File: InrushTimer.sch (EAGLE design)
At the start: 71 parts, among them IC2 TLC272D, IC3 4076N, IC6 555, Q2 TIP41C

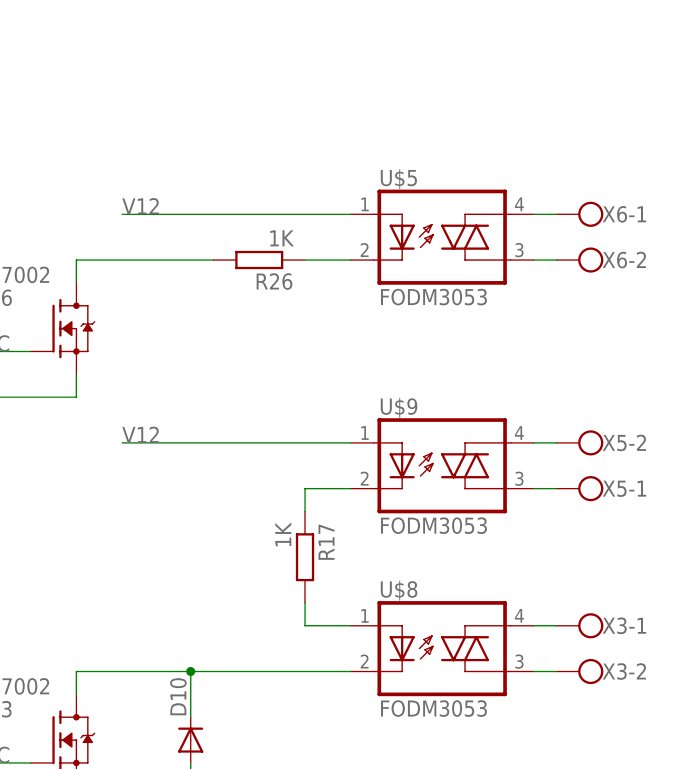
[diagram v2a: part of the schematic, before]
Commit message: Updated optotriac symbol
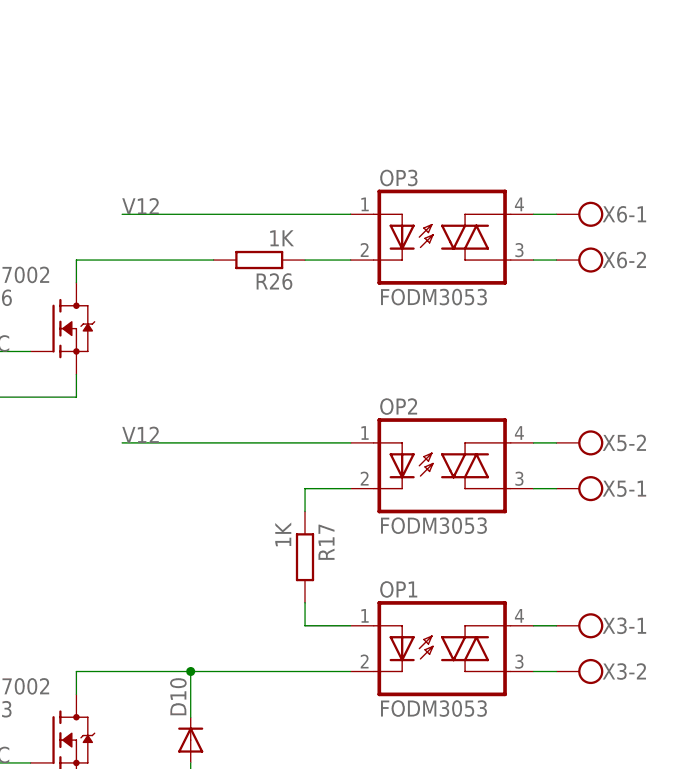
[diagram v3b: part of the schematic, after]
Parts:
- renumbered U$5 to OP3, U$8 to OP1, U$9 to OP2
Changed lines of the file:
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@@
 <part name="C4" library="rcl" deviceset="C-EU" device="050-024X044" value="100nF"/>
 <part name="C13" library="rcl" deviceset="C-EU" device="C1206K" value="100nF"/>
-<part name="U$5" library="SHoleLib" deviceset="FODM3053" device=""/>
 <part name="Q2" library="transistor-power" deviceset="TIP41C" device=""/>
 <part name="R17" library="rcl" deviceset="R-EU_" device="R0805" value="1K"/>
@@
 <part name="R24" library="rcl" deviceset="R-EU_" device="0207/7" value="51K"/>
 <part name="C11" library="rcl" deviceset="C-EU" device="050-024X044" value="100nF"/>
-<part name="U$8" library="SHoleLib" deviceset="FODM3053" device=""/>
 <part name="R25" library="pot" deviceset="TRIM_EU-" device="CA6H_MOD" value="220K"/>
 <part name="X3" library="con-wago-500" deviceset="W237-102" device=""/>
@@
 <part name="C3" library="rcl" deviceset="C-EU" device="050-024X044" value="100nF"/>
 <part name="IC6" library="linear" deviceset="*555" device=""/>
-<part name="U$9" library="SHoleLib" deviceset="FODM3053" device=""/>
 <part name="C7" library="rcl" deviceset="C-EU" device="C0805K" value="1nF"/>
 <part name="T2" library="transistor" deviceset="*-NPN-" device="SOT23-BEC" technology="MMBTA42LT1"/>
@@
 <part name="R18" library="rcl" deviceset="R-EU_" device="0207/2V" value="100R"/>
 <part name="R20" library="rcl" deviceset="R-EU_" device="0207/2V" value="10K"/>
+<part name="OP1" library="SHoleLib" deviceset="FODM3053" device=""/>
+<part name="OP2" library="SHoleLib" deviceset="FODM3053" device=""/>
+<part name="OP3" library="SHoleLib" deviceset="FODM3053" device=""/>
 </parts>
 <sheets>
@@
 <instance part="C4" gate="G$1" x="78.74" y="40.64"/>
 <instance part="C13" gate="G$1" x="132.08" y="106.68"/>
-<instance part="U$5" gate="G$1" x="518.16" y="27.94"/>
 <instance part="Q2" gate="1" x="83.82" y="50.8"/>
 <instance part="R17" gate="G$1" x="502.92" y="-7.62" rot="R270"/>
@@
 <instance part="R24" gate="G$1" x="292.1" y="-15.24" rot="R270"/>
 <instance part="C11" gate="G$1" x="226.06" y="-50.8"/>
-<instance part="U$8" gate="G$1" x="518.16" y="-17.78"/>
 <instance part="R25" gate="1" x="248.92" y="-35.56" rot="R90"/>
 <instance part="X3" gate="-1" x="535.94" y="-15.24" rot="R180"/>
@@
 <instance part="C3" gate="G$1" x="327.66" y="-10.16"/>
 <instance part="IC6" gate="A" x="210.82" y="-22.86"/>
-<instance part="U$9" gate="G$1" x="518.16" y="2.54"/>
 <instance part="C7" gate="G$1" x="119.38" y="124.46" rot="R90"/>
 <instance part="T2" gate="G$1" x="15.24" y="-5.08" smashed="yes">
@@
 <instance part="R18" gate="G$1" x="71.12" y="-20.32" rot="R180"/>
 <instance part="R20" gate="G$1" x="154.94" y="139.7"/>
+<instance part="OP1" gate="G$1" x="518.16" y="-17.78"/>
+<instance part="OP2" gate="G$1" x="518.16" y="2.54"/>
+<instance part="OP3" gate="G$1" x="518.16" y="27.94"/>
 </instances>
 <busses>
@@
 </segment>
 <segment>
-<pinref part="U$5" gate="G$1" pin="A"/>
 <wire x1="508" y1="30.48" x2="482.6" y2="30.48" width="0.1524" layer="91"/>
 <label x="482.6" y="30.48" size="1.778" layer="95"/>
+<pinref part="OP3" gate="G$1" pin="A"/>
 </segment>
 <segment>
@@
 </segment>
 <segment>
-<pinref part="U$9" gate="G$1" pin="A"/>
 <wire x1="508" y1="5.08" x2="482.6" y2="5.08" width="0.1524" layer="91"/>
 <label x="482.6" y="5.08" size="1.778" layer="95"/>
+<pinref part="OP2" gate="G$1" pin="A"/>
 </segment>
 </net>
@@
 <wire x1="490.22" y1="-20.32" x2="477.52" y2="-20.32" width="0.1524" layer="91"/>
 <wire x1="490.22" y1="-25.4" x2="490.22" y2="-20.32" width="0.1524" layer="91"/>
-<pinref part="U$8" gate="G$1" pin="C"/>
 <wire x1="490.22" y1="-20.32" x2="508" y2="-20.32" width="0.1524" layer="91"/>
 <junction x="490.22" y="-20.32"/>
+<pinref part="OP1" gate="G$1" pin="C"/>
 </segment>
 </net>
@@
 <segment>
 <pinref part="X6" gate="-2" pin="KL"/>
-<pinref part="U$5" gate="G$1" pin="A1"/>
 <wire x1="530.86" y1="25.4" x2="528.32" y2="25.4" width="0.1524" layer="91"/>
+<pinref part="OP3" gate="G$1" pin="A1"/>
 </segment>
 </net>
@@
 <segment>
 <pinref part="X6" gate="-1" pin="KL"/>
-<pinref part="U$5" gate="G$1" pin="A2"/>
 <wire x1="530.86" y1="30.48" x2="528.32" y2="30.48" width="0.1524" layer="91"/>
+<pinref part="OP3" gate="G$1" pin="A2"/>
 </segment>
 </net>
 <net name="N$18" class="0">
 <segment>
-<pinref part="U$5" gate="G$1" pin="C"/>
 <pinref part="R26" gate="G$1" pin="1"/>
 <wire x1="508" y1="25.4" x2="502.92" y2="25.4" width="0.1524" layer="91"/>
+<pinref part="OP3" gate="G$1" pin="C"/>
 </segment>
 </net>
@@
 <segment>
 <pinref part="X3" gate="-1" pin="KL"/>
-<pinref part="U$8" gate="G$1" pin="A2"/>
 <wire x1="528.32" y1="-15.24" x2="530.86" y2="-15.24" width="0.1524" layer="91"/>
+<pinref part="OP1" gate="G$1" pin="A2"/>
 </segment>
 </net>
@@
 <segment>
 <pinref part="X3" gate="-2" pin="KL"/>
-<pinref part="U$8" gate="G$1" pin="A1"/>
 <wire x1="528.32" y1="-20.32" x2="530.86" y2="-20.32" width="0.1524" layer="91"/>
+<pinref part="OP1" gate="G$1" pin="A1"/>
 </segment>
 </net>
 <net name="N$15" class="0">
 <segment>
-<pinref part="U$8" gate="G$1" pin="A"/>
 <pinref part="R17" gate="G$1" pin="2"/>
 <wire x1="508" y1="-15.24" x2="502.92" y2="-15.24" width="0.1524" layer="91"/>
 <wire x1="502.92" y1="-15.24" x2="502.92" y2="-12.7" width="0.1524" layer="91"/>
+<pinref part="OP1" gate="G$1" pin="A"/>
 </segment>
 </net>
 <net name="N$17" class="0">
 <segment>
-<pinref part="U$9" gate="G$1" pin="C"/>
 <pinref part="R17" gate="G$1" pin="1"/>
 <wire x1="508" y1="0" x2="502.92" y2="0" width="0.1524" layer="91"/>
 <wire x1="502.92" y1="0" x2="502.92" y2="-2.54" width="0.1524" layer="91"/>
+<pinref part="OP2" gate="G$1" pin="C"/>
 </segment>
 </net>
 <net name="N$20" class="0">
 <segment>
-<pinref part="U$9" gate="G$1" pin="A2"/>
 <pinref part="X5" gate="-2" pin="KL"/>
 <wire x1="530.86" y1="5.08" x2="528.32" y2="5.08" width="0.1524" layer="91"/>
+<pinref part="OP2" gate="G$1" pin="A2"/>
 </segment>
 </net>
 <net name="N$21" class="0">
 <segment>
-<pinref part="U$9" gate="G$1" pin="A1"/>
 <pinref part="X5" gate="-1" pin="KL"/>
 <wire x1="530.86" y1="0" x2="528.32" y2="0" width="0.1524" layer="91"/>
-</segment>
-</net>
+<pinref part="OP2" gate="G$1" pin="A1"/>
+</segment>
+</net>

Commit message: Fixed missing libraries by moving parts into local lib. Renumbered components.
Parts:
- removed C17: 100nF (DNF), rcl:C-EU050-024X044
- removed IC6: 555, linear:555
- removed R26: 1K, rcl:R-EU_R0805
- removed R28, R29: 200K, rcl:R-EU_0207/2V
- removed SJ2: (no value), jumper:SJ
- removed T2: (no value), transistor:MMBTA42LT1-NPN-SOT23-BEC
- removed U$13, U$3, U$6, U$7: 2N7002, transistor-fet:2N7002
- removed U$4: BU48XXG, ROHM_By_element14_Batch_1:BU48XXG
- removed X5, X6: (no value), con-wago-500:W237-102
- removed X7: (no value), con-wago-500:W237-103
- added C16: 100nF (DNF), rcl:C-EU050-024X044
- added IC1: TLC272D, linear:TLC272D
- added Q1: TIP41C, transistor-power:TIP41C
- added Q3, Q4, Q5: TRANSISTOR-FET_2N7002, InrushTimer:TRANSISTOR-FET_2N7002
- added R21: 10K, rcl:R-EU_0207/2V
- added R22, R23: 200K, rcl:R-EU_0207/2V
- added SJ1: (no value), jumper:SJ
- added T1: (no value), transistor:MMBTA42LT1-NPN-SOT23-BEC
- added U1: ROHM_BY_ELEMENT14_BATCH_1_BU48XXG, InrushTimer:ROHM_BY_ELEMENT14_BATCH_1_BU48XXG
- added X1: (no value), con-wago-500:W237-103
- added X2, X4: (no value), con-wago-500:W237-102
- C1: value 100nF -> 10uF; device rcl:C-EUC1206K -> rcl:CPOL-EUE2-5
- C10: value 1nF -> 10pF (DNF)
- C11, C4: value 100nF -> 10nF
- C12, C14: value 10nF -> 100nF
- C13: value 100nF -> 2.2uF
- C15: value 10pF (DNF) -> 100nF (DNF); device rcl:C-EUC0805K -> rcl:C-EU050-024X044
- C2: value 10uF -> 100nF; device rcl:CPOL-EUE2-5 -> rcl:C-EU050-024X044
- C3: value 100nF -> 100uF; device rcl:C-EU050-024X044 -> rcl:CPOL-EUE2.5-7
- C5: value 100uF -> 10nF; device rcl:CPOL-EUE2.5-7 -> rcl:C-EUC0805K
- C6: value 2.2uF -> 1nF; device rcl:C-EUC1206K -> rcl:C-EUC0805K
- C8: value 100nF (DNF) -> 100nF; device rcl:C-EU050-024X044 -> rcl:C-EUC1206K
- C9: value 10nF -> 100nF; device rcl:C-EUC0805K -> rcl:C-EUC1206K
- D1: value BZX55 -> Z12V; device diode:BZX55 -> diode:DIODE-SOD323-R
- D12: value BZX55 -> 1N4148DO35-7; device diode:BZX55 -> diode:1N4148DO35-7
- D2: value 1N4148DO35-7 -> BZX55; device diode:1N4148DO35-7 -> diode:BZX55
- D3: value Z12V -> BZX55; device diode:DIODE-SOD323-R -> diode:BZX55
- D4: value 1n4001 -> STTH110
- D5: value 1N4148DO35-7 -> 1n4001; device diode:1N4148DO35-7 -> diode:DIODE-DO41-10
- D7: value STTH110 -> 1N4148DO35-7; device diode:DIODE-DO41-10 -> diode:1N4148DO35-7
- IC2: value TLC272D -> 555; device linear:TLC272D -> linear:555
- Q2: value TIP41C -> TRANSISTOR-FET_2N7002; device transistor-power:TIP41C -> InrushTimer:TRANSISTOR-FET_2N7002
- R1: value 100K -> 4K7
- R10: value 9.1M -> 10K; device rcl:R-EU_0207/10 -> rcl:R-EU_0207/2V
- R12: value 200K -> 100K
- R13: value 100K -> 200K
- R14: value 22K -> 100K
- R15: value 51K -> 220K; device rcl:R-EU_0207/2V -> pot:TRIM_EU-CA6H_MOD
- R16: value 10K -> 1K
- R17: value 1K -> 51K; device rcl:R-EU_R0805 -> rcl:R-EU_0207/7
- R18: value 100R -> 10K
- R2: value 10K -> 27K
- R24: value 51K -> 1K; device rcl:R-EU_0207/7 -> rcl:R-EU_R0805
- R25: value 220K -> 1K; device pot:TRIM_EU-CA6H_MOD -> rcl:R-EU_R0805
- R4: value 4K7 -> 10K
- R5: value 10K -> 100R
- R7: value 27K -> 51K
- R8: value 1K -> 22K
- R9: value 10K -> 9.1M; device rcl:R-EU_0207/2V -> rcl:R-EU_0207/10
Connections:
- net DISABLE_A: now also D12.A, SJ1.2; no longer D10.A, SJ2.2
- net HYST: now also IC1A.-IN, R11.2; no longer IC2A.-IN, R13.2
- net N$1: now also D4.A, X1-1.KL; no longer D7.A, X7-1.KL
- net N$10: now also OP1.A2, X2-1.KL; no longer OP3.A2, X6-1.KL
- net N$11: now also C5.2, D4.C, D5.A, IC1B.+IN, R8.2; no longer C9.2, D4.A, D7.C, IC2B.+IN, R6.2
- net N$12: now also OP3.A1, X4-2.KL; no longer OP1.A1, X3-2.KL
- net N$13: now also R4.2, T1.E, U1.VDD; no longer R2.2, T2.E, U$4.VDD
- net N$14: now also C4.1, D2.C, R2.2, R3.2, T1.B; no longer C14.1, D12.C, R19.2, R7.2, T2.B
- net N$15: now also OP3.A, R25.2; no longer OP1.A, R17.2
- net N$16: now also D9.C, R18.1; no longer D2.C, R3.1
- net N$17: now also R25.1; no longer R17.1
- net N$18: now also OP1.C, R24.1; no longer OP3.C, R26.1
- net N$19: now also R20.2; no longer R5.2
- net N$2: now also R14.1, R15.E, R15.S; no longer R1.1, R25.E, R25.S
- net N$20: now also X3-2.KL; no longer X5-2.KL
- net N$21: now also X3-1.KL; no longer X5-1.KL
- net N$22: now also D8.C, R20.1; no longer D11.C, R5.1
- net N$23: now also R5.2, U1.VOUT; no longer R18.2, U$4.VOUT
- net N$24: now also D11.C, R21.1; no longer D9.C, R9.1
- net N$25: now also R19.2; no longer R16.2
- net N$26: now also IC1A.+IN, R10.2, R13.1; no longer IC2A.+IN, R11.1, R20.2
- net N$28: now also C13.2, IC2.DIS, IC2.THR, R15.A; no longer C6.2, IC6.DIS, IC6.THR, R25.A
- net N$3: now also R21.2; no longer R9.2
- net N$30: now also D10.C, R19.1; no longer D8.C, R16.1
- net N$31: now also Q4.D, R24.2; no longer R26.2, U$6.D
- net N$32: now also R18.2; no longer R3.2
- net N$36: now also Q3.G, R16.1; no longer R8.1, U$7.G
- net N$4: now also OP3.A2, X4-1.KL; no longer OP1.A2, X3-1.KL
- net N$40: now also C11.1, IC2.CV; no longer C12.1, IC6.CV
- net N$48: now also IC2.Q, R16.2; no longer IC6.Q, R8.2
- net N$5: now also OP1.A1, X2-2.KL; no longer OP3.A1, X6-2.KL
- net N$6: now also D12.C, OP3.C, Q5.D; no longer D10.C, OP1.C, U$3.D
- net N$7: now also C6.2, D7.A, IC1B.OUT, R10.1; no longer C10.2, D5.A, IC2B.OUT, R20.1
- net N$8: now also C2.1, D1.C, Q1.B, R1.1; no longer C4.1, D3.C, Q2.B, R4.1
- net N$9: now also C6.1, C9.1, D7.C, IC1B.-IN, R9.2; no longer C10.1, C13.1, D5.C, IC2B.-IN, R10.2
- net ON_A_SYNC: now also C15.2, D8.A, Q4.G, R22.2, SJ1.1; no longer C8.2, D9.A, R28.2, SJ2.1, U$6.G
- net ON_B: now also Q3.D, R17.2; no longer R24.2, U$7.D
- net ON_B_SYNC: now also C16.1, D10.A, D9.A, Q5.G, R23.2; no longer C17.1, D2.A, D8.A, R29.2, U$3.G
- net PEAK: now also C10.1, IC1A.OUT, R13.2; no longer C15.1, IC2A.OUT, R11.2
- net RECT: now also C1.+, Q1.C, R1.2, R2.1, T1.C, X1-2.KL; no longer C2.+, Q2.C, R4.2, R7.1, T2.C, X7-2.KL
- net RESET: now also Q2.D, R7.2; no longer R15.2, U$13.D
- net RESET_N: now also D3.C, IC2.R, IC2.TR, Q2.G, R5.1, R6.2; no longer D1.C, IC6.R, IC6.TR, R14.2, R18.1, U$13.G
- net V12: now also C12.1, C14.1, C3.+, C8.1, D5.C, IC1P.V+, IC2.V+, OP1.A, Q1.E, R11.1, R14.2, R17.1, R22.1, R23.1, R6.1, R7.1; no longer C1.1, C11.1, C3.1, C5.+, D4.C, IC2P.V+, IC6.V+, OP3.A, Q2.E, R1.2, R12.1, R14.1, R15.1, R24.1, R28.1, R29.1
- net ZERO: now also C1.-, C10.2, C13.1, C15.1, C16.2, C2.2, C3.-, C5.1, C8.2, C9.2, D2.A, IC1P.V-, IC2.GND, Q2.S, Q3.S, Q4.S, Q5.S, R12.1, R3.1, R4.1, R8.1, R9.1, U1.GND, X1-3.KL; no longer C1.2, C13.2, C15.2, C17.2, C2.-, C3.2, C5.-, C6.1, C8.1, C9.1, D12.A, IC2P.V-, IC6.GND, R10.1, R13.1, R19.1, R2.1, R6.1, U$13.S, U$3.S, U$4.GND, U$6.S, U$7.S, X7-3.KL
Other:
- moved on the sheet: C10, C11, C12, C13, C14, C15, C4, C6, C7, C8, C9, D10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

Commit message: Updated component packages
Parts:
- C15, C16: device rcl:C-EU050-024X044 -> rcl:C-EUC1206K
- R10, R18, R19, R20, R21, R4: device rcl:R-EU_0207/2V -> rcl:R-EU_R0805
- R16: device rcl:R-EU_0207/2V -> rcl:R-EU_R0402
- R24, R25: device rcl:R-EU_R0805 -> rcl:R-EU_0207/7
